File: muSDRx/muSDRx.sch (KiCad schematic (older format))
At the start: 89 parts, among them CON1 SJ1-3523N, CON2 SJ1-3523N, J1 Conn_01x02_Male, J11 Conn_01x02_Male, J2 Conn_01x02_Male, J3 Conn_01x02_Male, J4 Conn_01x02_Male, J5 Conn_01x02_Male, J6 Conn_01x02_Male, J9 Conn_01x04_Male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

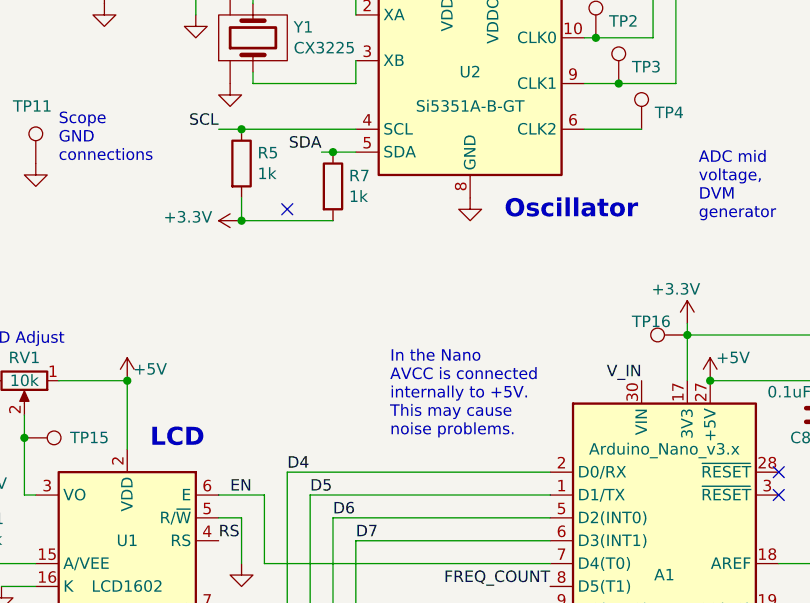
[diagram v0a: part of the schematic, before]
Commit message: Changed the sampling capacitors to 0.01uF for more bandwidth.
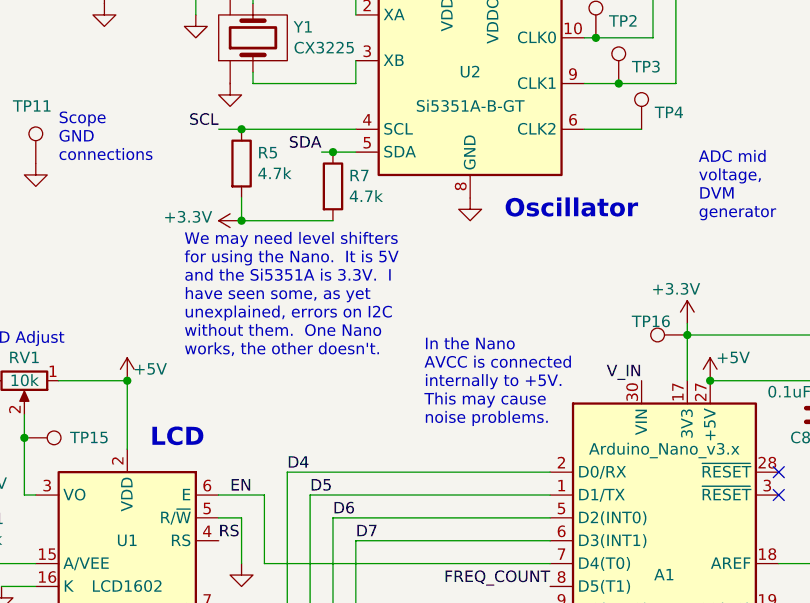
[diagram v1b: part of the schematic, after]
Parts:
- R5, R7: value 1k -> 4.7k
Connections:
- no-connect marks 25 -> 24
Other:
- note added: "We may need level shifters \nfor using the Nano. It is 5V \nand the Si5351A is 3.3V. I \nhave seen some, as yet \nunexplained, errors on I2C \nwithout them. One Nano\nworks, the other doesn't."
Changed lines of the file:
@@
 P 2400 3950
 F 0 "R7" H 2470 3996 50  0000 L CNN
-F 1 "1k" H 2470 3905 50  0000 L CNN
+F 1 "4.7k" H 2470 3905 50  0000 L CNN
 F 2 "Resistors_SMD:R_0805" V 2330 3950 50  0001 C CNN
 F 3 "~" H 2400 3950 50  0001 C CNN
@@
 P 2000 3850
 F 0 "R5" H 2070 3896 50  0000 L CNN
-F 1 "1k" H 2070 3805 50  0000 L CNN
+F 1 "4.7k" H 2070 3805 50  0000 L CNN
 F 2 "Resistors_SMD:R_0805" V 1930 3850 50  0001 C CNN
 F 3 "~" H 2000 3850 50  0001 C CNN
@@
 Text Label 5900 4950 2    50   ~ 0
 BUTTON
-Text Notes 2650 5050 0    50   ~ 0
+Text Notes 2800 5000 0    50   ~ 0
 In the Nano\nAVCC is connected \ninternally to +5V.  \nThis may cause\nnoise problems.
 Connection ~ 2450 1000
@@
 NoConn ~ 5900 5950
 NoConn ~ 4350 5300
-NoConn ~ 2200 4050
 $Comp
 L muSDRx-rescue:SJ1-3523N-dk_Barrel-Audio-Connectors CON2
@@
 Text Notes 4900 3200 0    50   ~ 0
 See note about BW above to the right.
+Text Notes 1750 4700 0    50   ~ 0
+We may need level shifters \nfor using the Nano.  It is 5V \nand the Si5351A is 3.3V.  I \nhave seen some, as yet \nunexplained, errors on I2C \nwithout them.  One Nano\nworks, the other doesn't.
 $EndSCHEMATC

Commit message: Committing to change to another branch
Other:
- note added: "0"
- note added: "180\n"
- note added: "270"
- note added: "90"
- note added: "Sequence of clocks: CLK1, CLK0\n0 degrees: 1,1\n90 degrees: 1,0\n180 degrees: 0,0\n270 degrees: 0,1"
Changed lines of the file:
@@
 Sheet 1 1
 Title "muSDRx Receiver"
-Date "2020-07-01"
-Rev "0.1"
+Date "2020-08-12"
+Rev "0.11"
 Comp "Rob Frohne, KL7NA"
 Comment1 "After µSDX: thanks to Guido, PE1NNZ"
@@
 Text Notes 2600 2050 0    50   ~ 0
 Antenna
-Wire Wire Line
-	950  1700 950  2200
 $Comp
 L power:GND #PWR04
@@
 Text Notes 1750 4700 0    50   ~ 0
 We may need level shifters \nfor using the Nano.  It is 5V \nand the Si5351A is 3.3V.  I \nhave seen some, as yet \nunexplained, errors on I2C \nwithout them.  One Nano\nworks, the other doesn't.
+Wire Wire Line
+	950  1700 950  2200
+Text Notes 6250 1750 0    50   ~ 0
+0
+Text Notes 6000 1550 0    50   ~ 0
+180\n
+Text Notes 6400 2250 0    50   ~ 0
+90
+Text Notes 6200 2600 0    50   ~ 0
+270
+Text Notes 5200 1300 0    50   ~ 0
+Sequence of clocks:  CLK1, CLK0\n0 degrees:   1,1\n90 degrees:  1,0\n180 degrees: 0,0\n270 degrees: 0,1
 $EndSCHEMATC

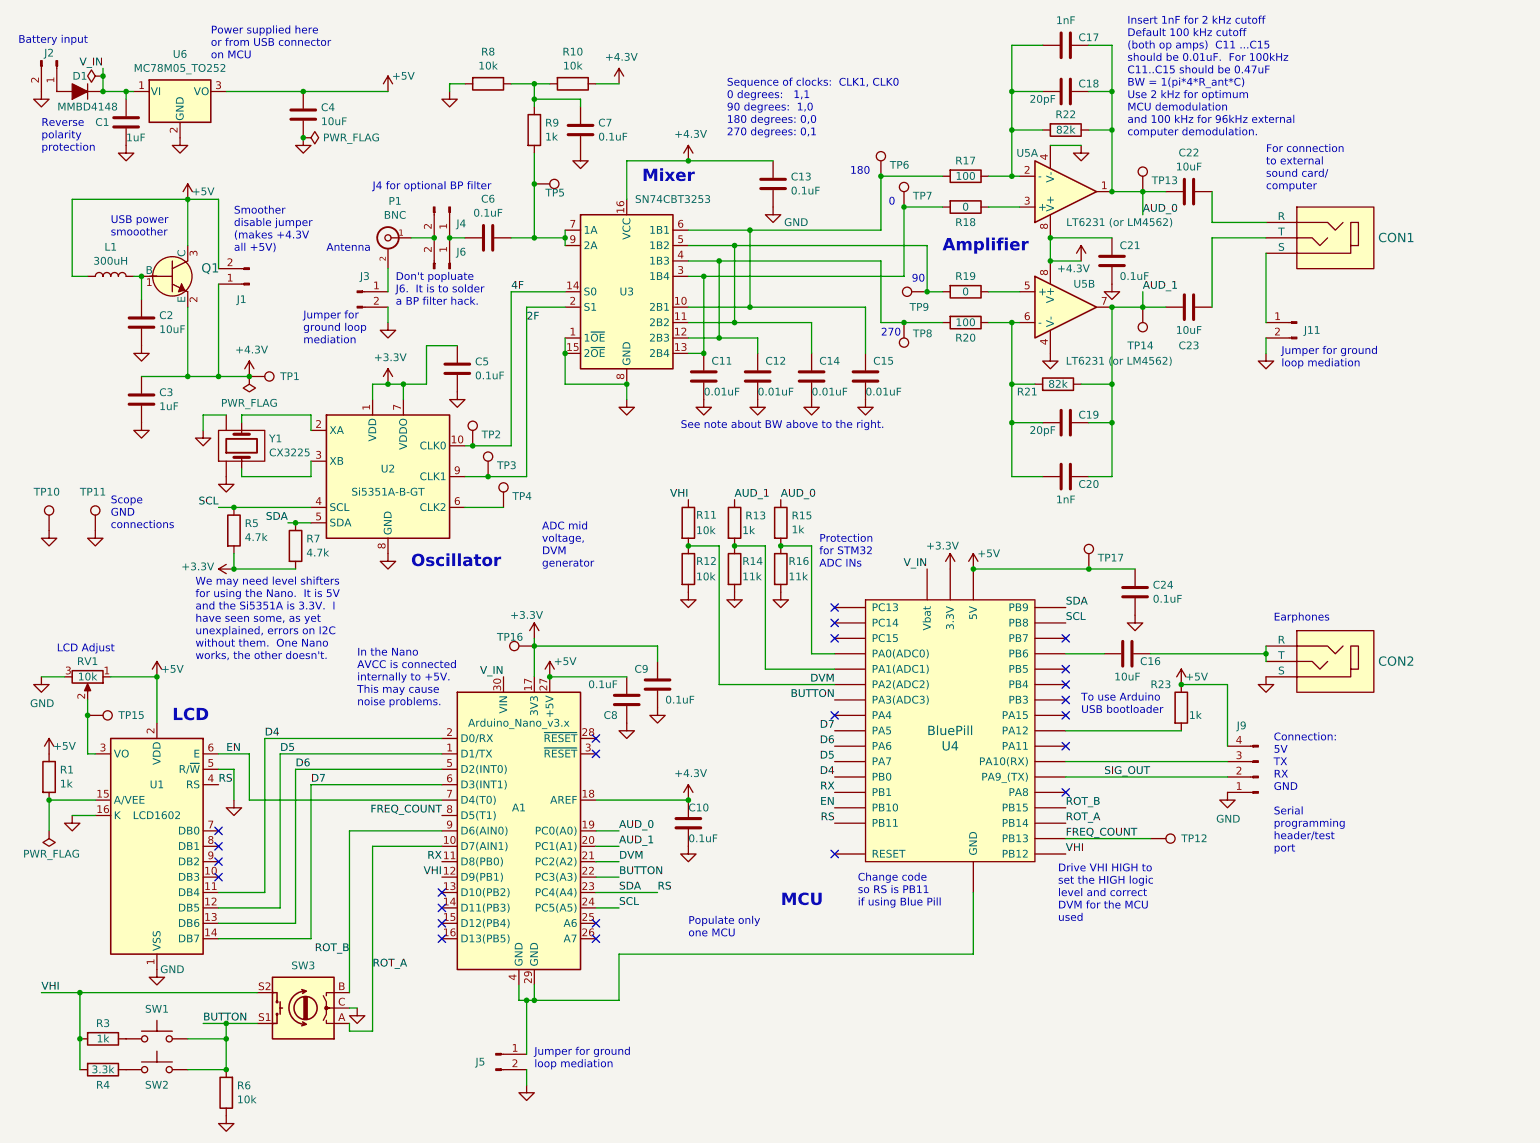
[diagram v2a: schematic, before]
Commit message: Added v0.11 which fixed problems wit stand alone using Nano
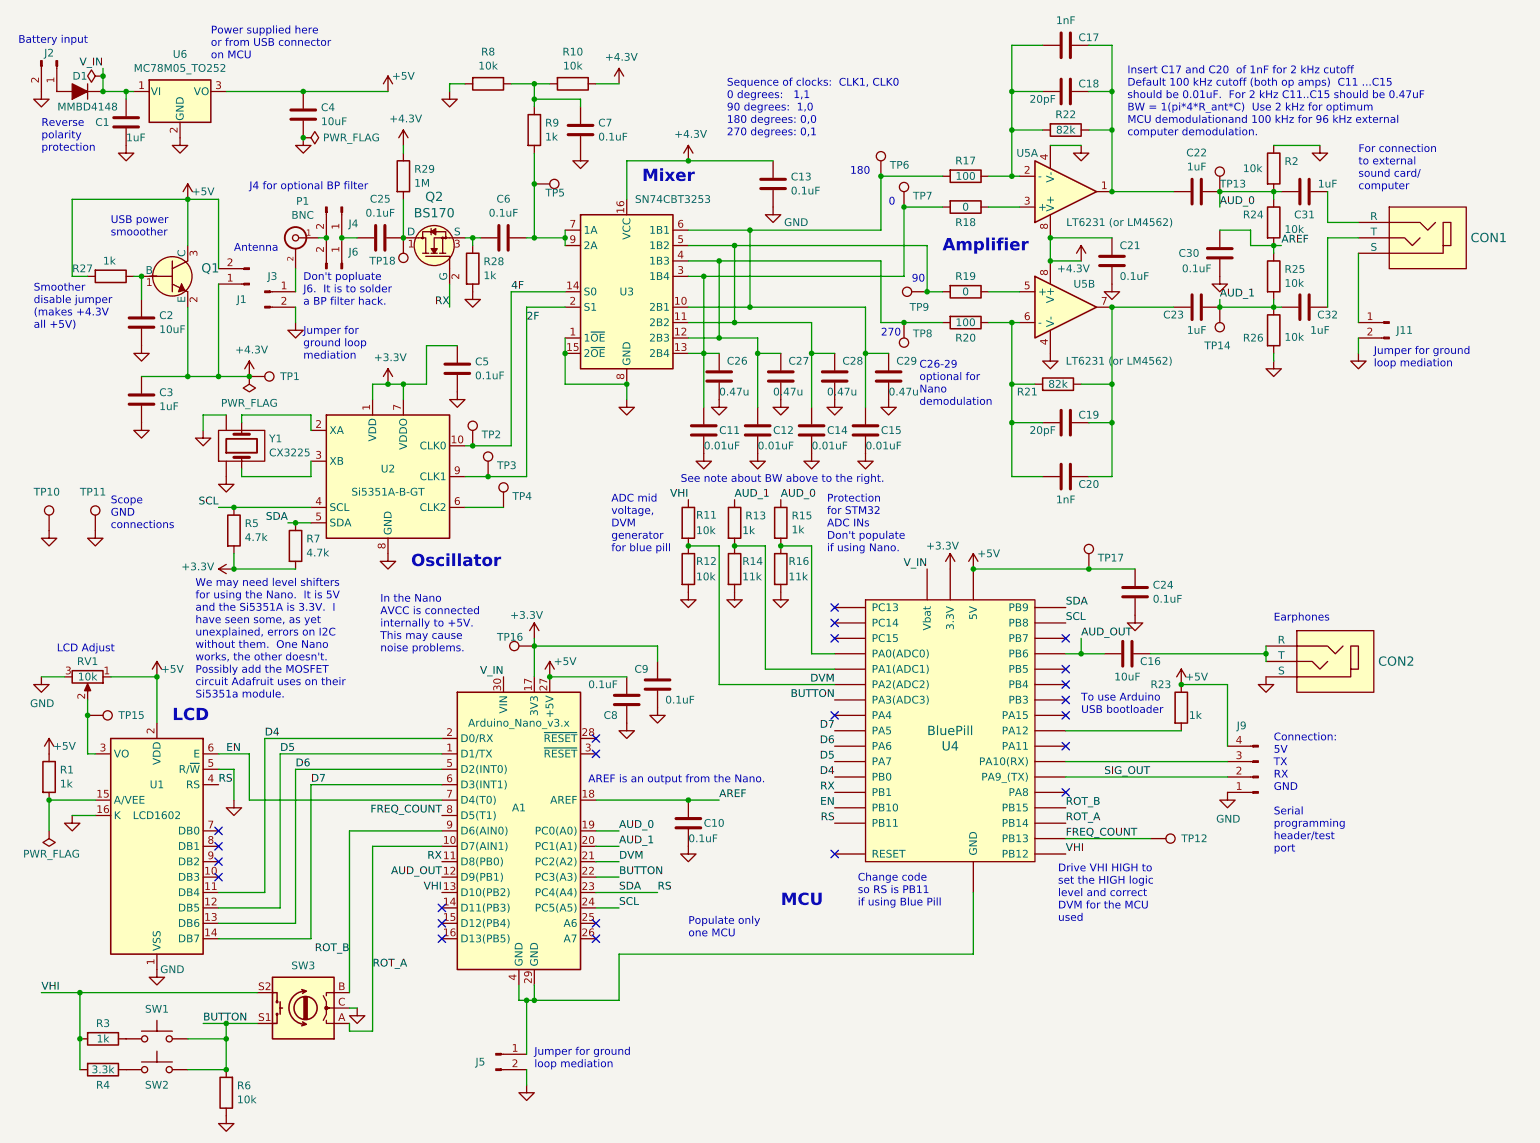
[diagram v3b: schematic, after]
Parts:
- removed L1: 300uH, Inductors_SMD:L_7.3x7.3_H4.5, symbol Device:L
- added C25, C30: 0.1uF, Capacitor_SMD:C_0805_2012Metric, symbol Device:C
- added C26, C27, C28, C29: 0.47u, Capacitor_SMD:C_0805_2012Metric, symbol Device:C
- added C31, C32: 1uF, Capacitor_SMD:C_0805_2012Metric, symbol Device:C
- added Q2: BS170, digikey-footprints:TO-92-3, symbol dk_Transistors-FETs-MOSFETs-Single:BS170
- added R2, R24, R25, R26: 10k, Resistor_SMD:R_0805_2012Metric, symbol Device:R
- added R27, R28: 1k, Resistor_SMD:R_0805_2012Metric, symbol Device:R
- added R29: 1M, Resistor_SMD:R_0805_2012Metric, symbol Device:R
- added TP18: TestPoint, TestPoint:TestPoint_THTPad_D1.5mm_Drill0.7mm, symbol muSDRx-rescue:TestPoint-Connector
- C17, C20: footprint Pin_Headers:Pin_Header_Straight_1x02_Pitch2.54mm -> Capacitor_SMD:C_0805_2012Metric
- C22, C23: value 10uF -> 1uF
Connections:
- net +4.3V: now also R29.1; no longer A1.18 (AREF), C10.1
- net +5V: now also R27.2
- net AUD_0: now also C22.1, C31.1, R2.2, R24.1; no longer C17.1, C18.1, C22.2, R22.1, U5.1
- net AUD_1: now also C23.1, C32.1, R25.2, R26.1; no longer C19.1, C20.1, C23.2, R21.1, U5.7
- net GND: now also C26.2, C27.2, C28.2, C29.2, C30.1, R2.1, R26.2, R28.2
- net RX: now also Q2.2 (G)
- net VHI: now also A1.13 (D10(PB2)); no longer A1.12 (D9(PB1))
- net at J4.1 (Pin_1), J6.1 (Pin_1): now also C25.2; no longer C6.2
- net at C15.1, R17.2, TP6.1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: now also C29.1
- net at C14.1, R19.2, TP9.1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: now also C28.1
- net at C12.1, R20.2, TP8.1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: now also C27.1
- net at C11.1, R18.2, TP7.1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: now also C26.1
- net at CON1.3 (R): now also C31.2; no longer C22.1
- net at CON1.2 (T): now also C32.2; no longer C23.1
- net at C2.1, Q1.1 (B): now also R27.1
- net AUD_OUT: now reaches C16.2, U4.PB6
- net AUD_OUT: now also A1.12 (D9(PB1))
- new net: C6.2, Q2.3 (S), R28.1
- new net: C17.1, C18.1, C22.2, R22.1, U5.1
- new net: C19.1, C20.1, C23.2, R21.1, U5.7
- new net: C25.1, Q2.1 (D), R29.2, TP18.1
- new net AREF: A1.18 (AREF), C10.1, C30.2, R24.2, R25.1
- no-connect marks 24 -> 23
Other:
- note added: "ADC mid\nvoltage,\nDVM\ngenerator\nfor blue pill"
- note added: "AREF is an output from the Nano."
- note added: "C26-29 \noptional for \nNano\ndemodulation"
- note added: "Insert C17 and C20 of 1nF for 2 kHz cutoff\nDefault 100 kHz cutoff (both op amps) C11 ...C15\nshould be 0.01uF. For 2 kHz C11..C15 should be 0.47uF\nBW = 1(pi*4*R_ant*C) Use 2 kHz for optimum \nMCU demodulationand 100 kHz for 96 kHz external\ncomputer demodulation."
- note added: "Protection\nfor STM32\nADC INs\nDon't populate \nif using Nano."
- note added: "We may need level shifters \nfor using the Nano. It is 5V \nand the Si5351A is 3.3V. I \nhave seen some, as yet \nunexplained, errors on I2C \nwithout them. One Nano\nworks, the other doesn't.\nPossibly add the MOSFET\ncircuit Adafruit uses on their\nSi5351a module."
- note removed: "ADC mid\nvoltage,\nDVM\ngenerator"
- note removed: "Insert 1nF for 2 kHz cutoff\nDefault 100 kHz cutoff\n(both op amps) C11 ...C15\nshould be 0.01uF. For 100kHz\nC11..C15 should be 0.47uF\nBW = 1(pi*4*R_ant*C)\nUse 2 kHz for optimum \nMCU demodulation\nand 100 kHz for 96kHz external\ncomputer demodulation."
- note removed: "Protection\nfor STM32\nADC INs"
- note removed: "We may need level shifters \nfor using the Nano. It is 5V \nand the Si5351A is 3.3V. I \nhave seen some, as yet \nunexplained, errors on I2C \nwithout them. One Nano\nworks, the other doesn't."
- moved on the sheet: C11, C12, C14, C15, C22, C23, C6, CON1, J11, J3, J4, J6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
